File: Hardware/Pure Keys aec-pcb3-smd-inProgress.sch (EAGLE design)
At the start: 71 parts, among them Q2 20MHz, T1 2N3904, U1 ATMEGA328P_TQFP, U2 LM4040

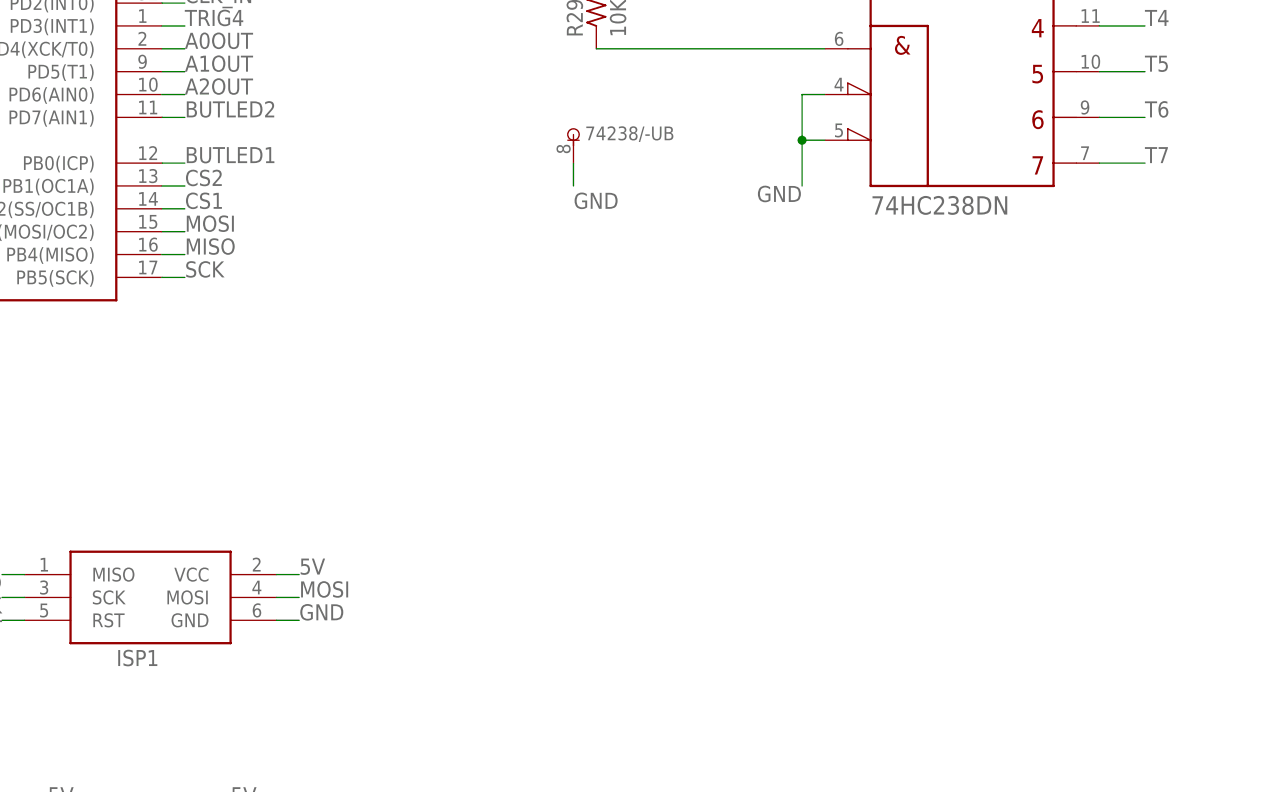
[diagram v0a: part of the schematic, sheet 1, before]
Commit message: changed cs select
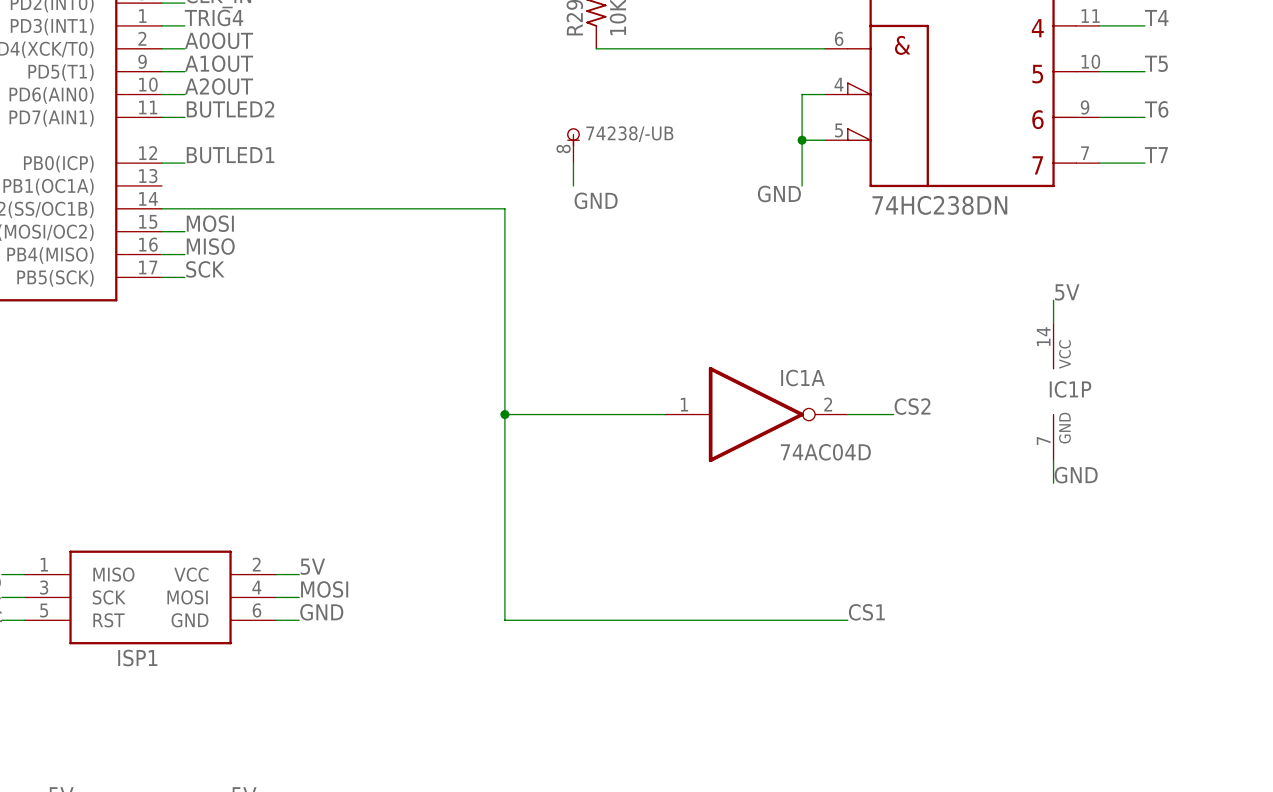
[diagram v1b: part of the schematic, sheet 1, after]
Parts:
- added IC1: 74AC04D, 74xx-eu:74AC04D
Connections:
- new net BUTLED3: BUT3G$2.A
- net 5V: now also IC1P.VCC
- net BUTLED1: no longer BUT3G$2.A
- net CS1: now also IC1A.I
- net CS2: now also IC1A.O; no longer U1.PB1(OC1A)
- net GND: now also IC1P.GND
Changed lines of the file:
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@@
 <part name="74238" library="GMSN-R2Project" deviceset="74HC238D" device="N"/>
 <part name="R29" library="rcl" deviceset="R-US_" device="R0805" value="10K"/>
+<part name="IC1" library="74xx-eu" library_urn="urn:adsk.eagle:library:85" deviceset="74*04" device="D" package3d_urn="urn:adsk.eagle:package:1010/2" technology="AC"/>
 </parts>
 <sheets>
@@
 <instance part="74238" gate="/-UB" x="111.76" y="121.92"/>
 <instance part="R29" gate="G$1" x="114.3" y="137.16" rot="R90"/>
+<instance part="IC1" gate="A" x="132.08" y="91.44"/>
+<instance part="IC1" gate="P" x="165.1" y="93.98"/>
 </instances>
 <busses>
@@
 <label x="137.16" y="116.84" size="1.778" layer="95" rot="R180"/>
 </segment>
+<segment>
+<pinref part="IC1" gate="P" pin="GND"/>
+<wire x1="165.1" y1="86.36" x2="165.1" y2="83.82" width="0.1524" layer="91"/>
+<label x="165.1" y="83.82" size="1.778" layer="95"/>
+</segment>
 </net>
 <net name="RST" class="0">
@@
 <net name="CS2" class="0">
 <segment>
-<wire x1="66.04" y1="116.84" x2="68.58" y2="116.84" width="0.1524" layer="91"/>
-<label x="68.58" y="116.84" size="1.778" layer="95"/>
-<pinref part="U1" gate="U$1" pin="PB1(OC1A)"/>
+<pinref part="IC1" gate="A" pin="O"/>
+<wire x1="142.24" y1="91.44" x2="147.32" y2="91.44" width="0.1524" layer="91"/>
+<label x="147.32" y="91.44" size="1.778" layer="95"/>
 </segment>
 </net>
@@
 <label x="114.3" y="144.78" size="1.778" layer="95" rot="R180"/>
 </segment>
+<segment>
+<pinref part="IC1" gate="P" pin="VCC"/>
+<wire x1="165.1" y1="101.6" x2="165.1" y2="104.14" width="0.1524" layer="91"/>
+<label x="165.1" y="104.14" size="1.778" layer="95"/>
+</segment>
 </net>
 <net name="MK4" class="0">
@@
 <net name="CS1" class="0">
 <segment>
-<wire x1="66.04" y1="114.3" x2="68.58" y2="114.3" width="0.1524" layer="91"/>
-<label x="68.58" y="114.3" size="1.778" layer="95"/>
 <pinref part="U1" gate="U$1" pin="PB2(SS/OC1B)"/>
+<wire x1="66.04" y1="114.3" x2="104.14" y2="114.3" width="0.1524" layer="91"/>
+<wire x1="104.14" y1="114.3" x2="104.14" y2="91.44" width="0.1524" layer="91"/>
+<wire x1="104.14" y1="91.44" x2="104.14" y2="68.58" width="0.1524" layer="91"/>
+<wire x1="104.14" y1="68.58" x2="142.24" y2="68.58" width="0.1524" layer="91"/>
+<pinref part="IC1" gate="A" pin="I"/>
+<wire x1="104.14" y1="91.44" x2="121.92" y2="91.44" width="0.1524" layer="91"/>
+<junction x="104.14" y="91.44"/>
+<label x="142.24" y="68.58" size="1.778" layer="95"/>
 </segment>
 </net>
@@
 <label x="99.06" y="66.04" size="1.778" layer="95" rot="R180"/>
 </segment>
-<segment>
-<pinref part="BUT3" gate="G$2" pin="A"/>
-<wire x1="99.06" y1="109.22" x2="109.22" y2="109.22" width="0.1524" layer="91"/>
-<label x="99.06" y="109.22" size="1.778" layer="95" rot="R180"/>
-</segment>
 </net>
 <net name="N$65" class="0">
@@
 </segment>
 </net>
+<net name="BUTLED3" class="0">
+<segment>
+<pinref part="BUT3" gate="G$2" pin="A"/>
+<wire x1="99.06" y1="109.22" x2="109.22" y2="109.22" width="0.1524" layer="91"/>
+<label x="99.06" y="109.22" size="1.778" layer="95" rot="R180"/>
+</segment>
+</net>

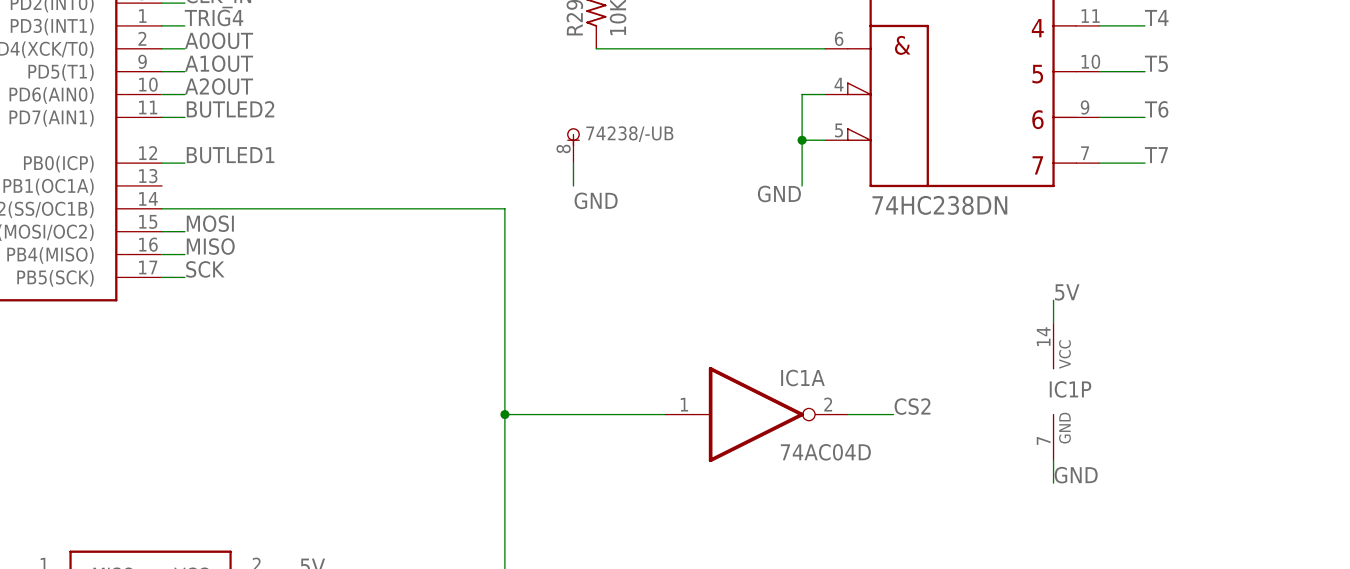
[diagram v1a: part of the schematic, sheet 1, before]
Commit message: New Board Shape and layout
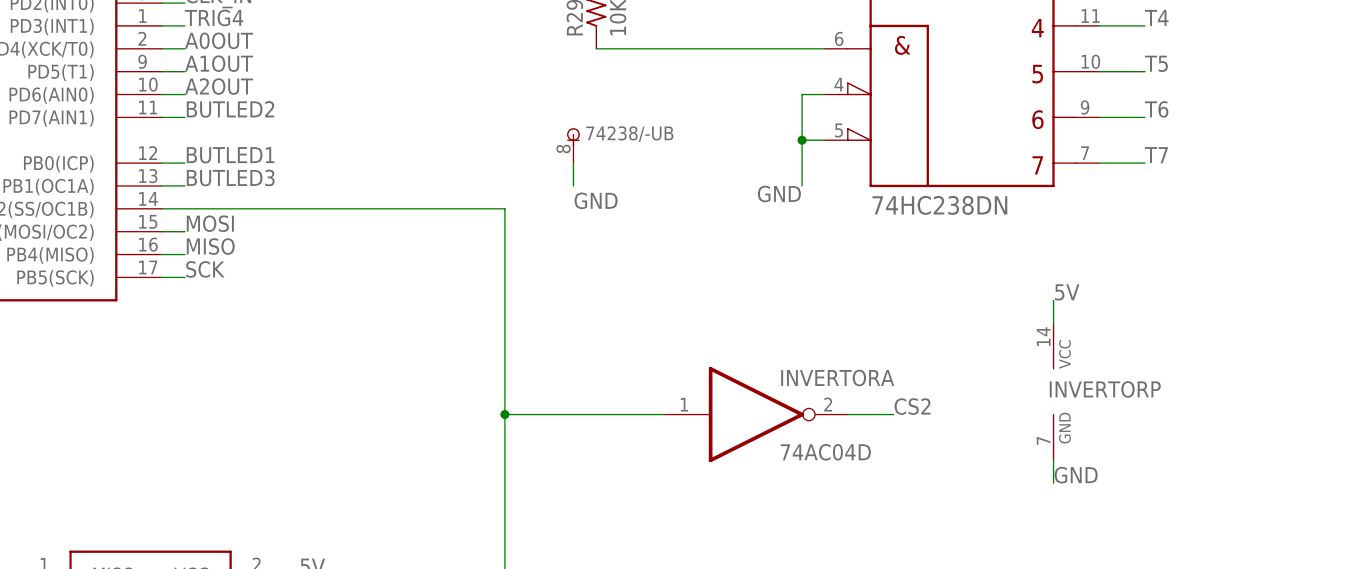
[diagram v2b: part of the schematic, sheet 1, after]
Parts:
- renumbered IC1 to INVERTOR, T1 to CLOCK, U2 to REF
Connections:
- net BUTLED3: now also U1.PB1(OC1A)
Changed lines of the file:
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@@
 <part name="BUT2" library="INSTRUO" deviceset="PB6149L-5" device=""/>
 <part name="R2" library="rcl" deviceset="R-US_" device="R0805" value="330R"/>
-<part name="T1" library="INSTRUO" deviceset="TRANSISTOR_MMBT3904" device="" value="2N3904"/>
+<part name="CLOCK" library="INSTRUO" deviceset="TRANSISTOR_MMBT3904" device="" value="2N3904"/>
 <part name="GND11" library="supply1" library_urn="urn:adsk.eagle:library:371" deviceset="GND" device=""/>
 <part name="R5" library="rcl" deviceset="R-US_" device="R0805" value="10K"/>
@@
 <part name="CLK_IN" library="GMSN" deviceset="PJ302M" device="" value="PJ302M"/>
 <part name="GND13" library="supply1" library_urn="urn:adsk.eagle:library:371" deviceset="GND" device=""/>
-<part name="U2" library="GMSN-R2Project" deviceset="LM4040A30IDBZT" device="" value="LM4040">
+<part name="REF" library="GMSN-R2Project" deviceset="LM4040A30IDBZT" device="" value="LM4040">
 <attribute name="MPN" value="LM4040A30IDBZT"/>
 <attribute name="RS-PART" value="809-6343"/>
@@
 <part name="74238" library="GMSN-R2Project" deviceset="74HC238D" device="N"/>
 <part name="R29" library="rcl" deviceset="R-US_" device="R0805" value="10K"/>
-<part name="IC1" library="74xx-eu" library_urn="urn:adsk.eagle:library:85" deviceset="74*04" device="D" package3d_urn="urn:adsk.eagle:package:1010/2" technology="AC"/>
+<part name="INVERTOR" library="74xx-eu" library_urn="urn:adsk.eagle:library:85" deviceset="74*04" device="D" package3d_urn="urn:adsk.eagle:package:1010/2" technology="AC"/>
 </parts>
 <sheets>
@@
 <instance part="74238" gate="/-UB" x="111.76" y="121.92"/>
 <instance part="R29" gate="G$1" x="114.3" y="137.16" rot="R90"/>
-<instance part="IC1" gate="A" x="132.08" y="91.44"/>
-<instance part="IC1" gate="P" x="165.1" y="93.98"/>
+<instance part="INVERTOR" gate="A" x="132.08" y="91.44"/>
+<instance part="INVERTOR" gate="P" x="165.1" y="93.98"/>
 </instances>
 <busses>
@@
 </segment>
 <segment>
-<pinref part="IC1" gate="P" pin="GND"/>
+<pinref part="INVERTOR" gate="P" pin="GND"/>
 <wire x1="165.1" y1="86.36" x2="165.1" y2="83.82" width="0.1524" layer="91"/>
 <label x="165.1" y="83.82" size="1.778" layer="95"/>
@@
 <net name="CS2" class="0">
 <segment>
-<pinref part="IC1" gate="A" pin="O"/>
+<pinref part="INVERTOR" gate="A" pin="O"/>
 <wire x1="142.24" y1="91.44" x2="147.32" y2="91.44" width="0.1524" layer="91"/>
 <label x="147.32" y="91.44" size="1.778" layer="95"/>
@@
 </segment>
 <segment>
-<pinref part="IC1" gate="P" pin="VCC"/>
+<pinref part="INVERTOR" gate="P" pin="VCC"/>
 <wire x1="165.1" y1="101.6" x2="165.1" y2="104.14" width="0.1524" layer="91"/>
 <label x="165.1" y="104.14" size="1.778" layer="95"/>
@@
 <wire x1="104.14" y1="91.44" x2="104.14" y2="68.58" width="0.1524" layer="91"/>
 <wire x1="104.14" y1="68.58" x2="142.24" y2="68.58" width="0.1524" layer="91"/>
-<pinref part="IC1" gate="A" pin="I"/>
+<pinref part="INVERTOR" gate="A" pin="I"/>
 <wire x1="104.14" y1="91.44" x2="121.92" y2="91.44" width="0.1524" layer="91"/>
 <junction x="104.14" y="91.44"/>
@@
 <wire x1="114.3" y1="132.08" x2="139.7" y2="132.08" width="0.1524" layer="91"/>
 <pinref part="74238" gate="1" pin="G1"/>
+</segment>
+</net>
+<net name="BUTLED3" class="0">
+<segment>
+<pinref part="U1" gate="U$1" pin="PB1(OC1A)"/>
+<wire x1="66.04" y1="116.84" x2="68.58" y2="116.84" width="0.1524" layer="91"/>
+<label x="68.58" y="116.84" size="1.778" layer="95"/>
 </segment>
 </net>
@@
 <instance part="C4" gate="G$1" x="43.18" y="43.18"/>
 <instance part="JP2" gate="G$1" x="25.4" y="38.1" rot="MR0"/>
-<instance part="U2" gate="A" x="119.38" y="40.64" rot="R90">
+<instance part="REF" gate="A" x="119.38" y="40.64" rot="R90">
 <attribute name="RS-PART" x="119.38" y="40.64" size="1.778" layer="96" rot="R90" display="off"/>
 </instance>
@@
 </segment>
 <segment>
-<pinref part="U2" gate="A" pin="ANODE"/>
+<pinref part="REF" gate="A" pin="ANODE"/>
 <wire x1="119.38" y1="35.56" x2="119.38" y2="30.48" width="0.1524" layer="91"/>
 <label x="119.38" y="30.48" size="1.778" layer="95" rot="R180"/>
@@
 <segment>
 <pinref part="R3" gate="G$1" pin="1"/>
-<pinref part="U2" gate="A" pin="CATHODE"/>
+<pinref part="REF" gate="A" pin="CATHODE"/>
 <wire x1="119.38" y1="53.34" x2="119.38" y2="48.26" width="0.1524" layer="91"/>
 <wire x1="119.38" y1="48.26" x2="119.38" y2="45.72" width="0.1524" layer="91"/>
@@
 </plain>
 <instances>
-<instance part="T1" gate="G$1" x="106.68" y="91.44" rot="R90"/>
+<instance part="CLOCK" gate="G$1" x="106.68" y="91.44" rot="R90"/>
 <instance part="GND11" gate="1" x="111.76" y="73.66" rot="MR0"/>
 <instance part="R5" gate="G$1" x="111.76" y="114.3" rot="MR90"/>
@@
 <net name="GND" class="1">
 <segment>
-<pinref part="T1" gate="G$1" pin="E"/>
+<pinref part="CLOCK" gate="G$1" pin="E"/>
 <wire x1="111.76" y1="78.74" x2="111.76" y2="76.2" width="0.1524" layer="91"/>
 <pinref part="GND11" gate="1" pin="GND"/>
@@
 <net name="CLK_IN" class="0">
 <segment>
-<pinref part="T1" gate="G$1" pin="C"/>
+<pinref part="CLOCK" gate="G$1" pin="C"/>
 <pinref part="R5" gate="G$1" pin="1"/>
 <wire x1="111.76" y1="109.22" x2="111.76" y2="106.68" width="0.1524" layer="91"/>
@@
 <wire x1="83.82" y1="91.44" x2="88.9" y2="91.44" width="0.1524" layer="91"/>
 <wire x1="88.9" y1="91.44" x2="88.9" y2="88.9" width="0.1524" layer="91"/>
-<pinref part="T1" gate="G$1" pin="B"/>
+<pinref part="CLOCK" gate="G$1" pin="B"/>
 <wire x1="93.98" y1="91.44" x2="88.9" y2="91.44" width="0.1524" layer="91"/>
 <junction x="88.9" y="91.44"/>
